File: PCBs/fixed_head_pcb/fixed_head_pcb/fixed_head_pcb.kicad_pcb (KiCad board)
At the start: 2 copper layers, 50.2 x 47.1 mm, 2 parts, among them J1 DB15_Female_HighDensity, U1 Pick_and_place_pcb

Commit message: modify kicad and freecad
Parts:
- moved J1 1.20 mm to (143.4, 49.0)
- moved U1 0.65 mm to (147.8, 70.2)
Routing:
- net pwm: track 51.7 -> 56.3 mm
- net SCL: track 35.4 -> 37.7 mm
- net limZ: track 41.5 -> 43.3 mm
- net SDA: track 29.0 -> 30.3 mm
- added copper zone on B.Cu, net +3V3
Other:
- outline, holes or cut-outs redrawn

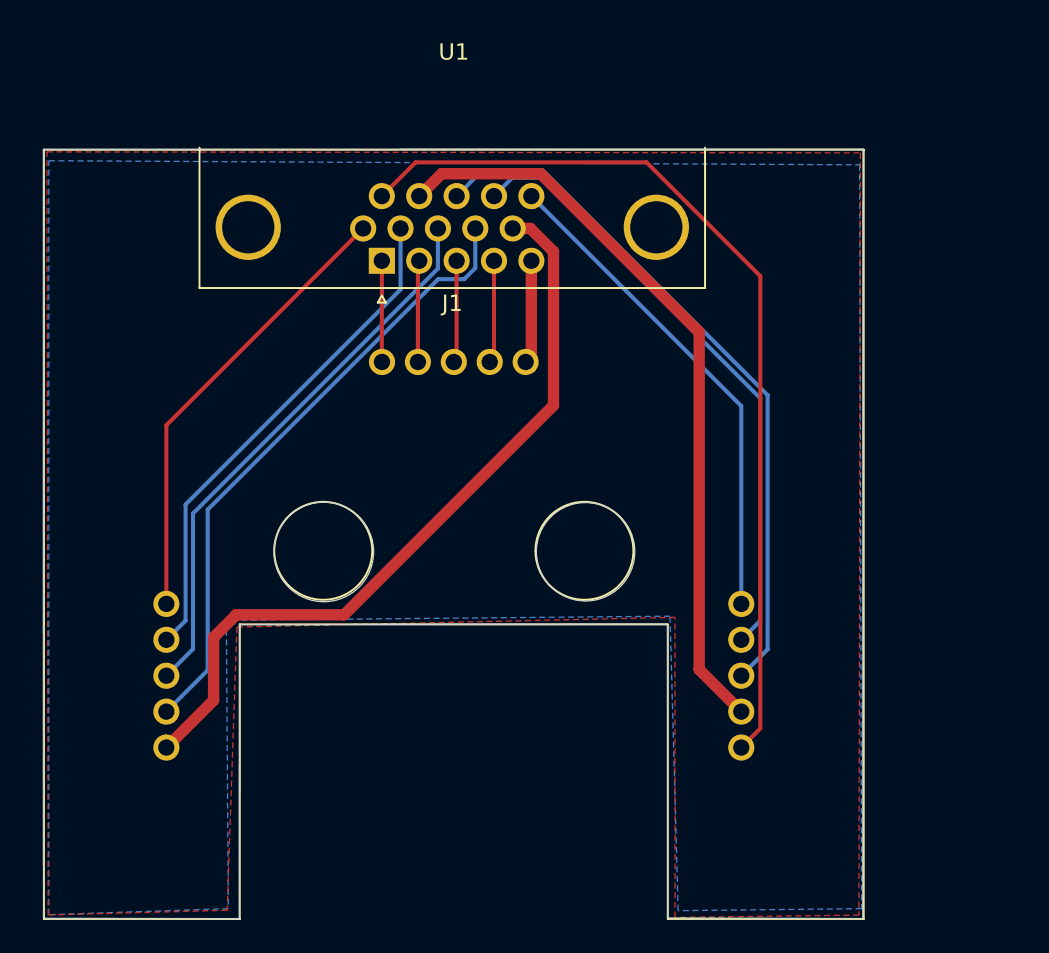
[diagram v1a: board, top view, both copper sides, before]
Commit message: add acrylic cut and other freecad design
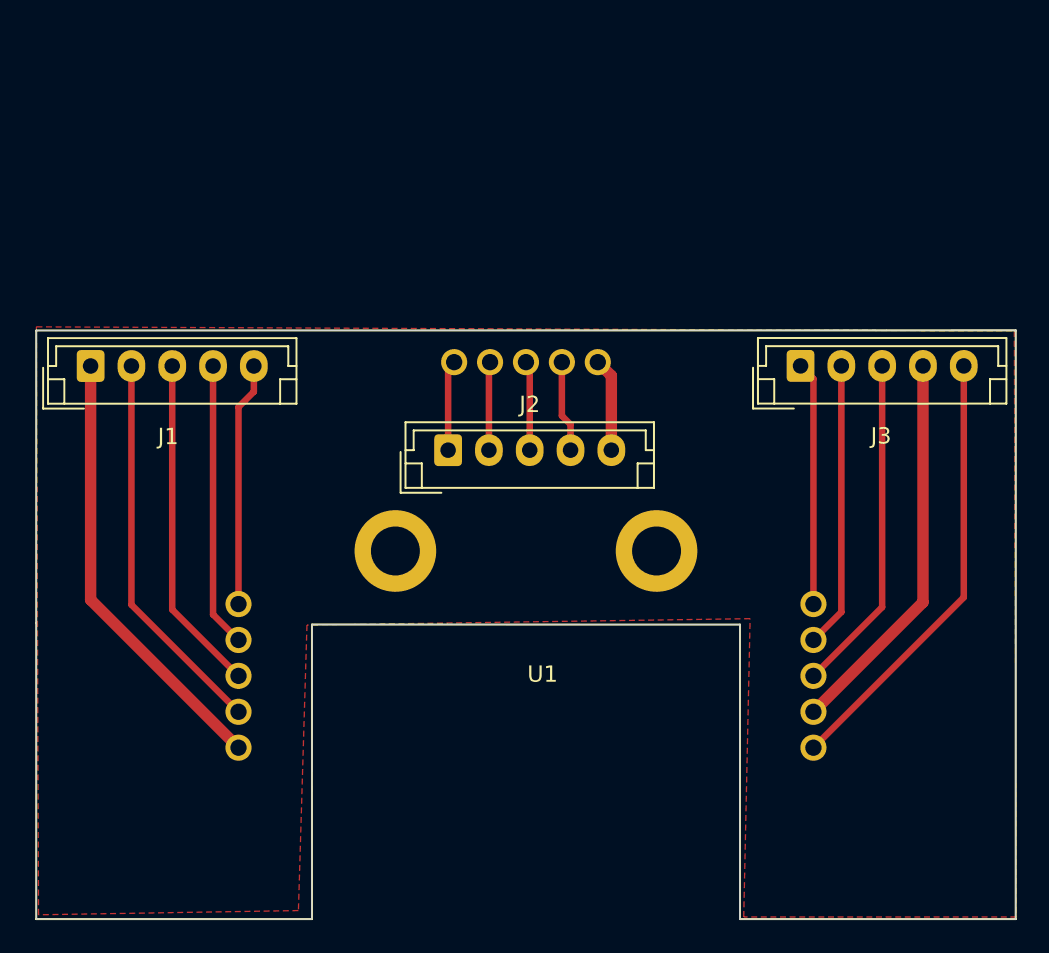
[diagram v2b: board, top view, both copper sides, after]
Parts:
- added J2: Conn_01x05, Connector_JST:JST_EH_B5B-EH-A_1x05_P2.50mm_Vertical, F.Cu at (147.4, 60.6)
- added J3: Conn_01x05, Connector_JST:JST_EH_B5B-EH-A_1x05_P2.50mm_Vertical, F.Cu at (169.0, 55.4)
- J1: value DB15_Female_HighDensity -> Conn_01x05; footprint Connector_Dsub:DSUB-15-HD_Female_Horizontal_P2.29x1.98mm_EdgePinOffset3.03mm_Housed_MountingHolesOffset4.94mm -> Connector_JST:JST_EH_B5B-EH-A_1x05_P2.50mm_Vertical
- moved J1 19.0 mm to (125.5, 55.4), turned to 0 degrees
- moved U1 4.42 mm to (152.2, 70.2)
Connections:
- J1 pad 1: A1A -> +3V3
- J1 pad 2: A2A -> Z2B
- J1 pad 3: A1B -> Z1B
- J1 pad 4: A2B -> Z2A
- J1 pad 5: +12V -> Z1A
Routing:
- net pwm: track 56.3 -> 27.2 mm
- net limZ: track 43.3 -> 20.7 mm
- net GND: track 46.1 -> 24.0 mm
- net SCL: track 37.7 -> 17.5 mm
- net +3V3: track 47.2 -> 27.1 mm
- net SDA: track 30.3 -> 14.9 mm
- net Z2B: track 38.4 -> 23.9 mm
- net Z2A: track 31.1 -> 17.4 mm
- net Z1B: track 34.3 -> 20.7 mm
- net Z1A: track 28.0 -> 15.0 mm
- net A2A: track 6.23 -> 5.42 mm
- net A1B: track 6.27 -> 5.49 mm
- net A2B: track 6.31 -> 5.61 mm
- net A1A: track 6.20 -> 5.55 mm
- net +12V: track 6.35 -> 5.74 mm
- removed copper zone on B.Cu, net +3V3
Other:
- board size 50.2 x 47.1 mm -> 60 x 36.1 mm
- net class Default: clearance 0.2 -> 0.4; trace_width 0.25 -> 0.4
- net class alim: clearance 0.2 -> 0.4
- rule trace_clearance: 0.2 -> 0.4

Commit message: update
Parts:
- moved J3 5.16 mm to (169.0, 60.6)
- moved J1 5.16 mm to (125.5, 60.6)
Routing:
- net SDA: track 14.9 -> 9.75 mm
- net pwm: track 27.2 -> 22.0 mm
- net limZ: track 20.7 -> 15.6 mm
- net SCL: track 17.5 -> 12.3 mm
- net Z2B: track 23.9 -> 18.7 mm
- net Z1B: track 20.7 -> 15.5 mm
- net Z1A: track 15.0 -> 9.82 mm
- net +3V3: track 27.1 -> 22.0 mm
- net GND: track 24.0 -> 18.9 mm
- net Z2A: track 17.4 -> 13.1 mm
- added copper zone on B.Cu, net GND
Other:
- board text added: "MagnetCnC"
- board text added: "Quetzhack"
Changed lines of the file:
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@@
   (general
     (thickness 1.6)
-    (drawings 8)
-    (tracks 32)
+    (drawings 10)
+    (tracks 35)
     (zones 0)
     (modules 4)
@@
     (visible_elements FFFFFF7F)
     (pcbplotparams
-      (layerselection 0x01000_7ffffffe)
+      (layerselection 0x010f0_ffffffff)
       (usegerberextensions false)
       (usegerberattributes true)
@@
   )
   (module Connector_JST:JST_EH_B5B-EH-A_1x05_P2.50mm_Vertical (layer F.Cu)
-    (at 125.522 55.4076)
+    (at 125.522 60.5638)
     (descr "JST EH series connector, B5B-EH-A (http://www.jst-mfg.com/product/pdf/eng/eEH.pdf), generated with kicad-footprint-generator")
     (tags "connector JST EH vertical")
@@
       (effects (font (size 1 1) (thickness 0.15)))
     )
-    (fp_text user %R (at 5 1.5) (layer F.Fab)
-      (effects (font (size 1 1) (thickness 0.15)))
-    )
     (fp_line (start -2.5 -1.6) (end -2.5 2.2) (layer F.Fab) (width 0.1))
     (fp_line (start -2.5 2.2) (end 12.5 2.2) (layer F.Fab) (width 0.1))
@@
     (fp_line (start -2.91 0.11) (end -2.91 2.61) (layer F.Fab) (width 0.1))
     (fp_line (start -2.91 2.61) (end -0.41 2.61) (layer F.Fab) (width 0.1))
+    (fp_text user %R (at 5 1.5) (layer F.Fab)
+      (effects (font (size 1 1) (thickness 0.15)))
+    )
     (pad 5 thru_hole oval (at 10 0) (size 1.7 1.95) (drill 0.95) (layers *.Cu *.Mask)
       (net 5 +12V))
@@
   )
   (module Connector_JST:JST_EH_B5B-EH-A_1x05_P2.50mm_Vertical (layer F.Cu)
-    (at 169.012 55.4025)
+    (at 169.012 60.5638)
     (descr "JST EH series connector, B5B-EH-A (http://www.jst-mfg.com/product/pdf/eng/eEH.pdf), generated with kicad-footprint-generator")
     (tags "connector JST EH vertical")
@@
     (pad 17 thru_hole circle (at -8 -3.4917) (size 5 5) (drill 3) (layers *.Cu *.Mask))
   )
+  (gr_text MagnetCnC (at 130.9116 84.84616) (layer F.SilkS)
+    (effects (font (size 1.5 1.5) (thickness 0.3)))
+  )
+  (gr_text Quetzhack (at 178.63312 81.4324 90) (layer F.SilkS)
+    (effects (font (size 1.5 1.5) (thickness 0.3)))
+  )
   (gr_line (start 122.19432 89.281) (end 122.19432 53.23332) (layer Edge.Cuts) (width 0.05))
   (gr_line (start 139.065 89.28608) (end 122.19432 89.281) (layer Edge.Cuts) (width 0.05))
@@
   (gr_line (start 182.20944 53.20792) (end 182.18912 89.28608) (layer Edge.Cuts) (width 0.05))
   (gr_line (start 122.19432 53.23332) (end 182.20944 53.20792) (layer Edge.Cuts) (width 0.05))
-  (segment (start 147.792 55.171) (end 147.422 55.541) (width 0.4) (layer F.Cu) (net 1))
-  (segment (start 147.422 55.541) (end 147.422 60.5638) (width 0.4) (layer F.Cu) (net 1))
-  (segment (start 149.992 55.171) (end 149.922 55.241) (width 0.4) (layer F.Cu) (net 2))
-  (segment (start 149.922 55.241) (end 149.922 60.5638) (width 0.4) (layer F.Cu) (net 2))
-  (segment (start 152.192 55.171) (end 152.422 55.401) (width 0.4) (layer F.Cu) (net 3))
-  (segment (start 152.422 55.401) (end 152.422 60.5638) (width 0.4) (layer F.Cu) (net 3))
-  (segment (start 154.922 60.5638) (end 154.922 58.9885) (width 0.4) (layer F.Cu) (net 4))
-  (segment (start 154.392 55.171) (end 154.392 58.4585) (width 0.4) (layer F.Cu) (net 4))
-  (segment (start 154.392 58.4585) (end 154.922 58.9885) (width 0.4) (layer F.Cu) (net 4))
-  (segment (start 156.592 55.171) (end 157.422 56.001) (width 0.7) (layer F.Cu) (net 5))
-  (segment (start 157.422 56.001) (end 157.422 60.5638) (width 0.7) (layer F.Cu) (net 5))
-  (segment (start 135.522 55.4076) (end 135.522 56.9829) (width 0.4) (layer F.Cu) (net 6))
-  (segment (start 134.582 69.991) (end 134.582 57.9229) (width 0.4) (layer F.Cu) (net 6))
-  (segment (start 134.582 57.9229) (end 135.522 56.9829) (width 0.4) (layer F.Cu) (net 6))
-  (segment (start 134.582 72.191) (end 133.022 70.631) (width 0.4) (layer F.Cu) (net 7))
-  (segment (start 133.022 70.631) (end 133.022 55.4076) (width 0.4) (layer F.Cu) (net 7))
+  (segment (start 147.792 60.1938) (end 147.422 60.5638) (width 0.4) (layer F.Cu) (net 1))
+  (segment (start 147.792 55.171) (end 147.792 60.1938) (width 0.4) (layer F.Cu) (net 1))
+  (segment (start 149.922 55.241) (end 149.992 55.171) (width 0.4) (layer F.Cu) (net 2))
+  (segment (start 149.922 60.5638) (end 149.922 55.241) (width 0.4) (layer F.Cu) (net 2))
+  (segment (start 152.192 60.3338) (end 152.422 60.5638) (width 0.4) (layer F.Cu) (net 3))
+  (segment (start 152.192 55.171) (end 152.192 60.3338) (width 0.4) (layer F.Cu) (net 3))
+  (segment (start 154.922 60.5638) (end 154.922 57.57904) (width 0.4) (layer F.Cu) (net 4))
+  (segment (start 154.392 57.04904) (end 154.392 55.171) (width 0.4) (layer F.Cu) (net 4))
+  (segment (start 154.922 57.57904) (end 154.392 57.04904) (width 0.4) (layer F.Cu) (net 4))
+  (segment (start 156.592 59.7338) (end 157.422 60.5638) (width 0.7) (layer F.Cu) (net 5))
+  (segment (start 156.592 55.171) (end 156.592 59.7338) (width 0.7) (layer F.Cu) (net 5))
+  (segment (start 134.582 69.991) (end 134.582 67.35816) (width 0.4) (layer F.Cu) (net 6))
+  (segment (start 135.522 66.41816) (end 135.522 60.5638) (width 0.4) (layer F.Cu) (net 6))
+  (segment (start 134.582 67.35816) (end 135.522 66.41816) (width 0.4) (layer F.Cu) (net 6))
+  (segment (start 133.022 60.5638) (end 133.022 65.40788) (width 0.4) (layer F.Cu) (net 7))
+  (segment (start 133.022 65.40788) (end 131.99364 66.43624) (width 0.4) (layer F.Cu) (net 7))
+  (segment (start 131.99364 69.60264) (end 134.582 72.191) (width 0.4) (layer F.Cu) (net 7))
+  (segment (start 131.99364 66.43624) (end 131.99364 69.60264) (width 0.4) (layer F.Cu) (net 7))
+  (segment (start 130.522 70.331) (end 130.522 60.5638) (width 0.4) (layer F.Cu) (net 8))
   (segment (start 134.582 74.391) (end 130.522 70.331) (width 0.4) (layer F.Cu) (net 8))
-  (segment (start 130.522 70.331) (end 130.522 55.4076) (width 0.4) (layer F.Cu) (net 8))
-  (segment (start 134.582 76.591) (end 128.022 70.031) (width 0.4) (layer F.Cu) (net 9))
-  (segment (start 128.022 70.031) (end 128.022 55.4076) (width 0.4) (layer F.Cu) (net 9))
+  (segment (start 128.022 70.031) (end 134.582 76.591) (width 0.4) (layer F.Cu) (net 9))
+  (segment (start 128.022 60.5638) (end 128.022 70.031) (width 0.4) (layer F.Cu) (net 9))
+  (segment (start 125.522 69.731) (end 125.522 60.5638) (width 0.7) (layer F.Cu) (net 10))
   (segment (start 134.582 78.791) (end 125.522 69.731) (width 0.7) (layer F.Cu) (net 10))
-  (segment (start 125.522 69.731) (end 125.522 55.4076) (width 0.7) (layer F.Cu) (net 10))
-  (segment (start 169.802 78.791) (end 179.012 69.581) (width 0.4) (layer F.Cu) (net 11))
-  (segment (start 179.012 69.581) (end 179.012 55.4025) (width 0.4) (layer F.Cu) (net 11))
-  (segment (start 169.802 76.591) (end 176.512 69.881) (width 0.7) (layer F.Cu) (net 12))
-  (segment (start 176.512 69.881) (end 176.512 55.4025) (width 0.7) (layer F.Cu) (net 12))
-  (segment (start 169.802 74.391) (end 174.012 70.181) (width 0.4) (layer F.Cu) (net 13))
-  (segment (start 174.012 70.181) (end 174.012 55.4025) (width 0.4) (layer F.Cu) (net 13))
+  (segment (start 179.012 69.581) (end 169.802 78.791) (width 0.4) (layer F.Cu) (net 11))
+  (segment (start 179.012 60.5638) (end 179.012 69.581) (width 0.4) (layer F.Cu) (net 11))
+  (segment (start 169.896002 76.591) (end 169.802 76.591) (width 0.7) (layer F.Cu) (net 12))
+  (segment (start 176.512 69.975002) (end 169.896002 76.591) (width 0.7) (layer F.Cu) (net 12))
+  (segment (start 176.512 60.5638) (end 176.512 69.975002) (width 0.7) (layer F.Cu) (net 12))
+  (segment (start 174.012 70.181) (end 169.802 74.391) (width 0.4) (layer F.Cu) (net 13))
+  (segment (start 174.012 60.5638) (end 174.012 70.181) (width 0.4) (layer F.Cu) (net 13))
+  (segment (start 171.512 70.481) (end 171.512 60.5638) (width 0.4) (layer F.Cu) (net 14))
   (segment (start 169.802 72.191) (end 171.512 70.481) (width 0.4) (layer F.Cu) (net 14))
-  (segment (start 171.512 70.481) (end 171.512 55.4025) (width 0.4) (layer F.Cu) (net 14))
-  (segment (start 169.802 69.991) (end 169.802 56.1925) (width 0.4) (layer F.Cu) (net 15))
-  (segment (start 169.802 56.1925) (end 169.012 55.4025) (width 0.4) (layer F.Cu) (net 15))
+  (segment (start 169.012 69.201) (end 169.802 69.991) (width 0.4) (layer F.Cu) (net 15))
+  (segment (start 169.012 60.5638) (end 169.012 69.201) (width 0.4) (layer F.Cu) (net 15))
   (zone (net 12) (net_name GND) (layer F.Cu) (hatch edge 0.508)
-    (connect_pads (clearance 0.6))
+    (connect_pads (clearance 0.508))
     (min_thickness 0.254)
     (fill yes (arc_segments 32) (thermal_gap 0.508) (thermal_bridge_width 0.508))
     (polygon
       (pts
-        (xy 182.10784 53.26888) (xy 182.23484 89.15908) (xy 165.5318 89.15908) (xy 165.92296 70.88632) (xy 138.77544 71.27748)
-        (xy 138.2522 88.76792) (xy 122.33148 89.027) (xy 122.1994 53.0098)
+        (xy 181.89956 89.01684) (xy 165.46068 89.13368) (xy 165.57752 71.40448) (xy 138.63828 71.17588) (xy 138.63828 88.9)
+        (xy 122.19432 89.36736) (xy 122.6312 53.48732) (xy 181.96052 53.2892)
       )
     )
+  )
+  (zone (net 12) (net_name GND) (layer B.Cu) (hatch edge 0.508)
+    (connect_pads (clearance 0.508))
+    (min_thickness 0.254)
+    (fill yes (arc_segments 32) (thermal_gap 0.508) (thermal_bridge_width 0.508))
+    (polygon
+      (pts
+        (xy 181.55412 88.66632) (xy 165.69436 89.01684) (xy 165.46068 70.82536) (xy 138.28776 70.70852) (xy 139.22248 89.36736)
+        (xy 122.07748 89.01684) (xy 122.77852 53.32984) (xy 181.55412 53.32984)
+      )
+    )
